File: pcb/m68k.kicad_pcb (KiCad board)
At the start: 2 copper layers, 100 x 100 mm, 116 parts, among them J1 USB_B_Micro, J2 Mini-DIN-6, J4 DB15_Male_HighDensity, J8 Micro_SD_Card, U1 93LC56, U10 25LCxxx, U11 TXB0108DQSR, U12 TXB0108DQSR, U13 iCE40-HX4K-TQ144, U14 ADV7125KSTZ50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

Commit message: Done?
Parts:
- moved C58 4.67 mm to (82.2, 58.8), turned to 90 degrees
- moved C33 1.68 mm to (79.2, 58.8), turned to 90 degrees
- moved C21 0.85 mm to (92.7, 53.5)
- moved C22 0.84 mm to (92.7, 52.0)
- moved C15 0.57 mm to (80.7, 58.8), turned to 90 degrees
- moved C67 0.29 mm to (92.7, 59.5)
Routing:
- net GND: track 708.6 -> 715.8 mm
- net +3V3: track 459.0 -> 452.7 mm, vias 49 -> 46
- net clk12: track 71.5 -> 69.7 mm, vias 8 -> 2
- net +1V2: track 128.0 -> 129.4 mm, vias 7 -> 6
- net +5V: track 346.3 -> 346.1 mm, vias 15 -> 14
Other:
- rule trace_min: 0.125 -> 0.127
- rule via_min_size: 0.4 -> 0.6

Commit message: Erik
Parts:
- moved R23 0.29 mm to (116.7, 105.2)
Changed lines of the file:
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@@
     (thickness 1.6)
     (drawings 12)
-    (tracks 2533)
+    (tracks 2534)
     (zones 0)
     (modules 116)
@@
   )
   (module Resistor_SMD:R_0603_1608Metric (layer F.Cu)
-    (at 116.712 104.9634)
+    (at 116.712 105.25)
     (descr "Resistor SMD 0603 (1608 Metric), square (rectangular) end terminal, IPC_7351 nominal, (Body size source: http://www.tortai-tech.com/upload/download/2011102023233369053.pdf), generated with kicad-footprint-generator")
     (tags resistor)
@@
   (via (at 117.55 102.15) (size 0.6) (drill 0.3) (layers F.Cu B.Cu) (net 1))
   (segment (start 117.4995 102.2005) (end 117.55 102.15) (width 0.2) (layer F.Cu) (net 1))
-  (segment (start 117.4995 103.6934) (end 117.4995 102.2005) (width 0.2) (layer F.Cu) (net 1))
   (via (at 114.55 103.4) (size 0.6) (drill 0.3) (layers F.Cu B.Cu) (net 1))
   (segment (start 114.5076 103.4424) (end 114.55 103.4) (width 0.2) (layer F.Cu) (net 1))
@@
   (segment (start 117.724 90.8878) (end 117.724 92.9492) (width 0.3) (layer F.Cu) (net 1))
   (segment (start 116.8181 89.9819) (end 117.724 90.8878) (width 0.3) (layer F.Cu) (net 1))
-  (segment (start 117.897 105.3609) (end 117.4995 104.9634) (width 0.3) (layer F.Cu) (net 1))
-  (segment (start 117.897 107.6574) (end 117.897 105.3609) (width 0.3) (layer F.Cu) (net 1))
-  (segment (start 117.4995 104.9634) (end 117.4995 103.6934) (width 0.3) (layer F.Cu) (net 1))
   (via (at 79.6 104.05) (size 0.6) (drill 0.3) (layers F.Cu B.Cu) (net 1))
   (segment (start 79.571 102.765) (end 79.571 104.021) (width 0.127) (layer F.Cu) (net 1))
@@
   (segment (start 80.7 56.75) (end 91.95 56.75) (width 0.127) (layer F.Cu) (net 1))
   (segment (start 91.95 56.75) (end 91.95 52.75) (width 0.127) (layer F.Cu) (net 1))
+  (segment (start 117.897 105.6475) (end 117.4995 105.25) (width 0.127) (layer F.Cu) (net 1))
+  (segment (start 117.897 107.6574) (end 117.897 105.6475) (width 0.127) (layer F.Cu) (net 1))
+  (segment (start 117.4995 103.6934) (end 117.4995 102.2005) (width 0.2) (layer F.Cu) (net 1))
+  (segment (start 117.4995 105.25) (end 117.4995 103.6934) (width 0.127) (layer F.Cu) (net 1))
   (segment (start 106.52036 86.98984) (end 106.52036 86.41484) (width 0.2) (layer F.Cu) (net 2))
   (segment (start 106.52036 87.16566) (end 106.52036 86.98984) (width 0.2) (layer F.Cu) (net 2))
@@
   (segment (start 74.3375 55.5) (end 73.25 55.5) (width 0.127) (layer F.Cu) (net 9))
   (segment (start 115.597 113.9574) (end 115.597 107.6574) (width 0.3) (layer F.Cu) (net 9))
-  (segment (start 115.9245 104.9634) (end 115.9245 103.6934) (width 0.3) (layer F.Cu) (net 9))
   (segment (start 115.9245 107.3299) (end 115.597 107.6574) (width 0.3) (layer F.Cu) (net 9))
-  (segment (start 115.9245 104.9634) (end 115.9245 107.3299) (width 0.3) (layer F.Cu) (net 9))
   (via (at 113.2 101.65) (size 0.6) (drill 0.3) (layers F.Cu B.Cu) (net 9))
   (segment (start 115.9245 103.6934) (end 113.8811 101.65) (width 0.2) (layer F.Cu) (net 9))
@@
   (segment (start 95.6625 50.5) (end 88.2 50.5) (width 0.127) (layer F.Cu) (net 9))
   (via (at 88.2 55.5) (size 0.6) (drill 0.3) (layers F.Cu B.Cu) (net 9))
+  (segment (start 115.597 105.5775) (end 115.9245 105.25) (width 0.127) (layer F.Cu) (net 9))
+  (segment (start 115.597 107.6574) (end 115.597 105.5775) (width 0.127) (layer F.Cu) (net 9))
+  (segment (start 115.9245 105.25) (end 115.9245 103.6934) (width 0.127) (layer F.Cu) (net 9))
   (segment (start 98.98 84.0226) (end 98.9855 84.0171) (width 0.2) (layer F.Cu) (net 10))
   (segment (start 98.105 84.0226) (end 98.98 84.0226) (width 0.2) (layer F.Cu) (net 10))

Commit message: vanity
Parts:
- added H1: MountingHole_Pad, MountingHole:MountingHole_2.5mm_Pad, F.Cu at (116.7, 33.5)
- added H2: MountingHole_Pad, MountingHole:MountingHole_2.5mm_Pad, F.Cu at (23.3, 116.5)
- added H3: MountingHole_Pad, MountingHole:MountingHole_2.5mm_Pad, F.Cu at (23.1, 23.2)
- added R8: 10k, Resistor_SMD:R_0603_1608Metric, F.Cu at (98.1, 62.6)
- moved C29 4.40 mm to (199.8, 46.3)
- moved C61 1.25 mm to (189.7, 54.1)
- moved C65 0.25 mm to (68.5, 67.8)
- moved C27 0.18 mm to (74.1, 67.7)
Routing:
- net GND: track 715.8 -> 773.9 mm
- net Net-(R10-Pad1): track 34.4 -> 37.7 mm
- net +3V3: track 452.7 -> 454.6 mm, vias 46 -> 47
- net Net-(R8-Pad2): track 31.9 -> 33.5 mm
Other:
- outline, holes or cut-outs redrawn
- board text added: "m68k Mr. Maas AP Physics 2019 Avery Bartnik Erik Duxstad Jack Sweeney Michael Wagner"

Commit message: Finished
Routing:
- net ADDR_OE: track 78.3 -> 87.1 mm
- net GND: track 773.9 -> 776.4 mm
- net +5V: track 346.0 -> 348.3 mm, vias 14 -> 13
- net /A23: track 57.0 -> 56.2 mm
- net /A10: track 35.8 -> 36.4 mm

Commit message: pre pour
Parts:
- removed C25, C26: 10uF, Capacitor_SMD:C_0603_1608Metric
- removed C28, C29: 1uF, Capacitor_SMD:C_0603_1608Metric
- removed C31, C32, C35, C39: 0.1uF, Capacitor_SMD:C_0603_1608Metric
- removed C57, C59, C61: 0.01uF, Capacitor_SMD:C_0603_1608Metric
- added H4: MountingHole_Pad, MountingHole:MountingHole_2.2mm_M2_Pad, F.Cu at (110.5, 117.4)
- C38, C41: moved to B.Cu
- moved C38 111.4 mm to (78.5, 56.5), turned to 0 degrees
- moved C41 95.9 mm to (93.5, 49.0), turned to 90 degrees
- moved C34 93.8 mm to (95.1, 39.4), turned to 90 degrees
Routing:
- net GND: track 776.4 -> 802.7 mm, vias 59 -> 60
- net +1V2: track 129.8 -> 133.2 mm, vias 6 -> 7
- net +3V3: track 454.6 -> 456.6 mm
- net Net-(J2-Pad1): track 102.2 -> 101.3 mm
- net +5V: track 348.3 -> 349.0 mm
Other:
- outline, holes or cut-outs redrawn
- board text added: "2019-05"
- board text added: "Mr. Maas Physics Avery Bartnik Erik Duxstad Jack Sweeney Michael Wagner"
- board text added: "m68k"
- board text removed: "m68k Mr. Maas AP Physics 2019 Avery Bartnik Erik Duxstad Jack Sweeney Michael Wagner"

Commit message: ordered
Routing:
- added copper zone on B.Cu, net GND
- added copper zone on F.Cu, net GND
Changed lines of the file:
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@@
       (outputformat 1)
       (mirror false)
-      (drillshape 1)
+      (drillshape 0)
       (scaleselection 1)
       (outputdirectory ""))
@@
     (tags "LQFP QFP")
     (attr smd)
-    (fp_text reference U3 (at 0.03 -0.0774) (layer F.SilkS)
+    (fp_text reference U3 (at -7.895 -3.7024) (layer F.SilkS)
       (effects (font (size 1 1) (thickness 0.15)))
     )
@@
     (tags "SSOP 0.65")
     (attr smd)
-    (fp_text reference U8 (at 0 4.95) (layer B.SilkS)
+    (fp_text reference U8 (at -4.75 4.725) (layer B.SilkS)
       (effects (font (size 1 1) (thickness 0.15)) (justify mirror))
     )
@@
     (tags "SSOP 0.65")
     (attr smd)
-    (fp_text reference U7 (at 0 4.95) (layer B.SilkS)
+    (fp_text reference U7 (at -4.425 4.85) (layer B.SilkS)
       (effects (font (size 1 1) (thickness 0.15)) (justify mirror))
     )
@@
     (tags capacitor)
     (attr smd)
-    (fp_text reference C69 (at 1.4079 1.5123) (layer F.SilkS)
+    (fp_text reference C69 (at 2.4079 0.2123 90) (layer F.SilkS)
       (effects (font (size 1 1) (thickness 0.15)))
     )
@@
     (tags "SOIC SO")
     (attr smd)
-    (fp_text reference U1 (at -0.0783 -0.0096 90) (layer F.SilkS)
+    (fp_text reference U1 (at -4.3533 -3.5096 180) (layer F.SilkS)
       (effects (font (size 1 1) (thickness 0.15)))
     )
@@
     (tags "TSOP I 32")
     (attr smd)
-    (fp_text reference U9 (at 0.35 -0.15) (layer F.SilkS)
+    (fp_text reference U9 (at -11.025 6.925 90) (layer F.SilkS)
       (effects (font (size 1 1) (thickness 0.15)))
     )
@@
     (tags "SMD SMT crystal oscillator")
     (attr smd)
-    (fp_text reference X1 (at 2.4117 -0.053) (layer F.SilkS)
+    (fp_text reference X1 (at -5.0883 3.047) (layer F.SilkS)
       (effects (font (size 1 1) (thickness 0.15)))
     )
@@
   (segment (start 98.3659 70.3159) (end 97.11621 69.06621) (width 0.2) (layer F.Cu) (net 244))
   (segment (start 97.11621 69.06621) (end 94.56621 69.06621) (width 0.2) (layer F.Cu) (net 244))
+  (zone (net 1) (net_name GND) (layer F.Cu) (hatch edge 0.508)
+    (connect_pads (clearance 0.508))
+    (min_thickness 0.254)
+    (fill yes (arc_segments 32) (thermal_gap 0.508) (thermal_bridge_width 0.508))
+    (polygon
+      (pts
+        (xy 21.25 117.65) (xy 21.25 22.65) (xy 23.25 20.65) (xy 117.25 20.65) (xy 119.25 22.65)
+        (xy 119.25 116.65) (xy 115.25 118.65) (xy 23.25 118.65)
+      )
+    )
+  )
+  (zone (net 1) (net_name GND) (layer B.Cu) (hatch edge 0.508)
+    (connect_pads (clearance 0.508))
+    (min_thickness 0.254)
+    (fill yes (arc_segments 32) (thermal_gap 0.508) (thermal_bridge_width 0.508))
+    (polygon
+      (pts
+        (xy 21.25 116.65) (xy 21.25 22.65) (xy 23.25 20.65) (xy 117.25 20.65) (xy 119.25 22.65)
+        (xy 119.25 116.65) (xy 115.25 118.65) (xy 23.25 118.65)
+      )
+    )
+  )
 )

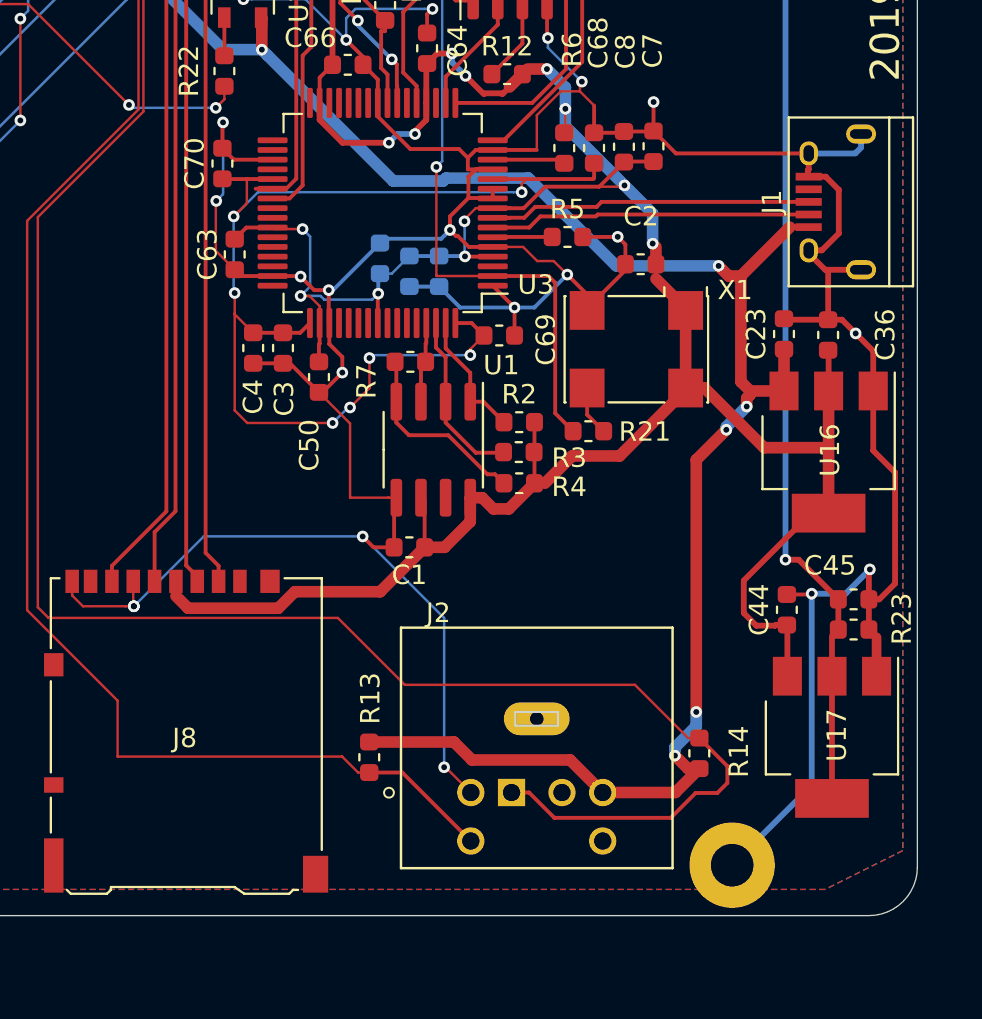
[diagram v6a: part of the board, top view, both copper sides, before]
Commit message: update ps/2, usb, and mounting hole.
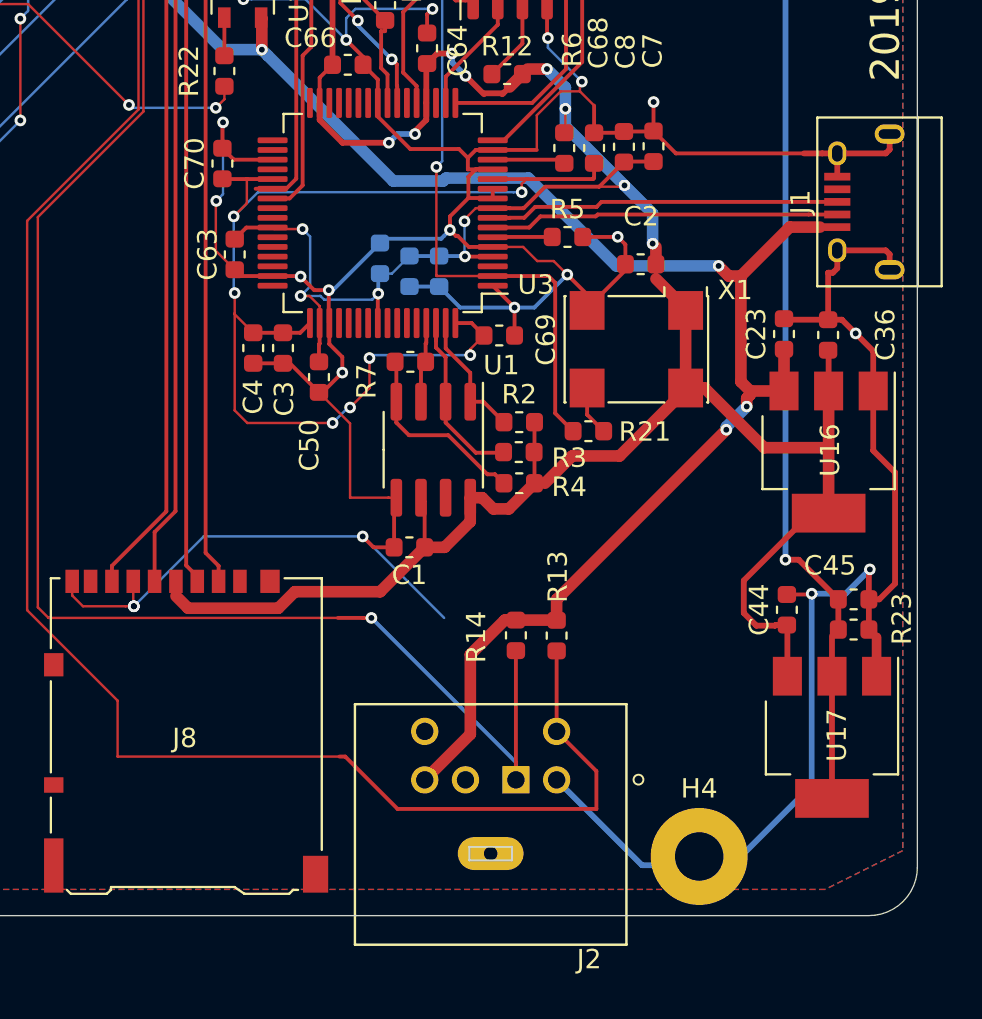
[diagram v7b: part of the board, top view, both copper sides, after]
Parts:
- H4: footprint MountingHole:MountingHole_2.2mm_M2_Pad -> MountingHole:MountingHole_2.5mm_Pad
- moved R13 11.5 mm to (101.4, 105.6)
- moved R14 11.2 mm to (99.3, 105.5), turned to 270 degrees
- moved J2 4.61 mm to (98.0, 115.3), turned to 180 degrees
- moved H4 1.76 mm to (108.8, 117.0)
- moved J1 1.47 mm to (117.2, 83.2)
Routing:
- net Net-(J2-Pad1): track 101.3 -> 84.6 mm, vias 0 -> 1
- net Net-(J2-Pad5): track 78.9 -> 93.9 mm
- net +5V: track 349.0 -> 338.6 mm, vias 13 -> 11
- net Net-(J1-Pad3): track 16.6 -> 18.1 mm
- net Net-(J1-Pad2): track 16.6 -> 18.0 mm
- net GND: track 802.7 -> 801.4 mm, vias 60 -> 59

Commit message: update resistor value
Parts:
- R5: value 2.2k -> 12k
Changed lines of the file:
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@@
   )
   (setup
-    (last_trace_width 0.6)
+    (last_trace_width 0.2)
     (user_trace_width 0.127)
     (user_trace_width 0.3)
@@
       (effects (font (size 1 1) (thickness 0.15)))
     )
-    (fp_text value 2.2k (at 0 1.43) (layer F.Fab)
+    (fp_text value 12k (at 0 1.43) (layer F.Fab)
       (effects (font (size 1 1) (thickness 0.15)))
     )
